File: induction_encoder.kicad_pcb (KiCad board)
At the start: 4 copper layers, 136 x 136 mm, 70 parts, among them J2 Conn_01x06, U1 MT9105ET, U10 IPS2200, U11 ADS1115IDGS, U12 ADS1115IDGS, U2 MT9105ET, U3 MT9105ET, U4 MT9105ET, U5 MT9105ET, U6 MT9105ET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

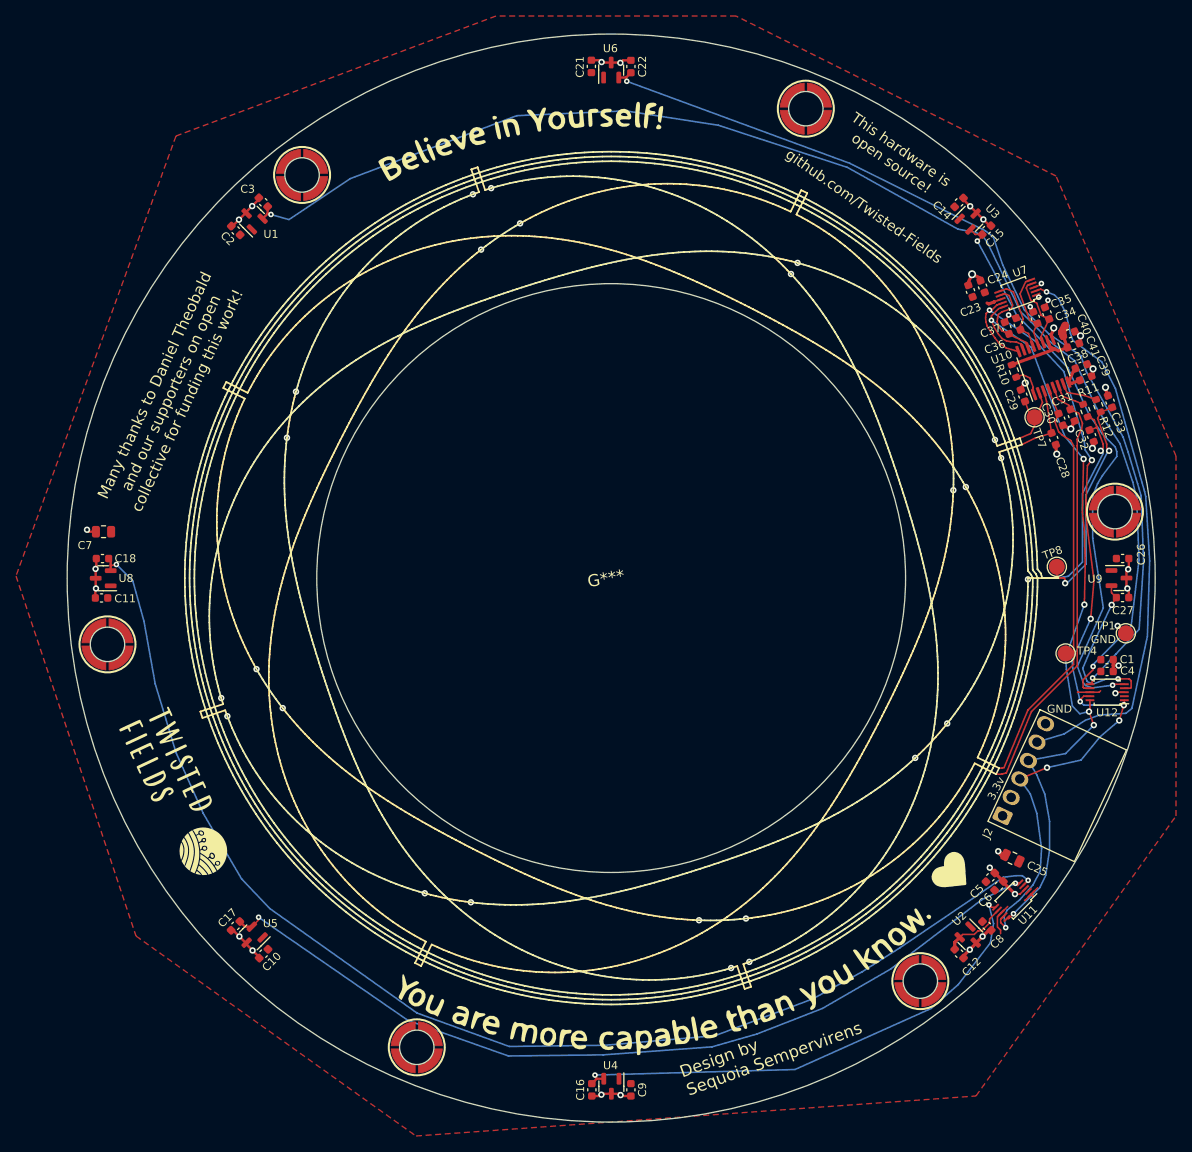
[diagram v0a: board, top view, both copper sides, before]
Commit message: Update to rev 2, add I2C pullups and updated silk
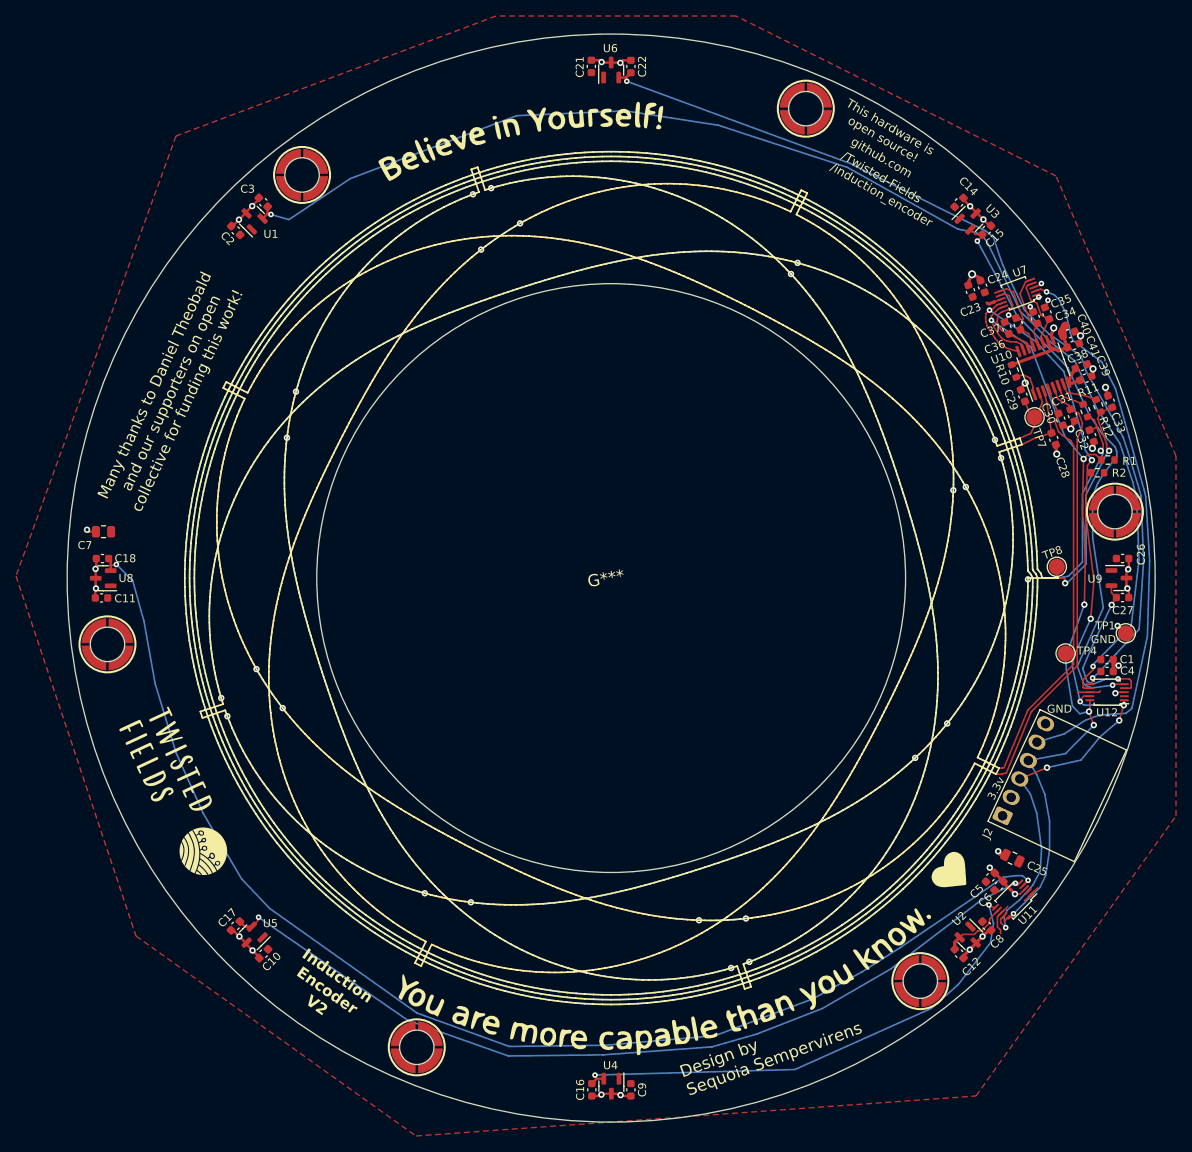
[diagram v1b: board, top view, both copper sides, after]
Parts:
- added R1: 5.1k, Resistor_SMD:R_0603_1608Metric, F.Cu at (162.1, 85.2)
- added R2: 5.1k, Resistor_SMD:R_0603_1608Metric, F.Cu at (160.8, 86.8)
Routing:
- net SCL: track 99.3 -> 102.1 mm
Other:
- board text added: "/Twisted-Fields"
- board text added: "/induction_encoder"
- board text added: "Induction Encoder V2"
- board text added: "github.com"
- board text removed: "github.com/Twisted-Fields"

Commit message: Update induction encoder for order placed July 2024
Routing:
- net RDY: track 70.7 -> 72.5 mm, vias 1 -> 2
- net SDA: track 113.2 -> 113.8 mm
- net SCL: track 102.1 -> 102.6 mm, vias 6 -> 8
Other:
- board text added: "Design by Sequoia Hope Alexander"
- board text removed: "Design by Sequoia Sempervirens"
